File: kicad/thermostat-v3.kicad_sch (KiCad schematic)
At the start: 91 parts, among them J1 HVAC R C W Y G, J2 USB-C, J3 Stemma QT, J4 2.9in EPD FPC, Q1 SI1308EDL, Q2 BT136S-600D, Q3 BT136S-600D, Q4 BT136S-600D, SW1 RESET, SW2 BOOT, SW3 UP, SW4 DOWN, SW5 MODE, U1 LMR16006XDDCR, U2 USBLC6-2SC6, U3 ESP32-C6-WROOM-1-N8, U4 STWD100NYWY3F, U5 SHT40-AD1B, U6 MOC3063S, U7 MOC3063S, U8 MOC3063S

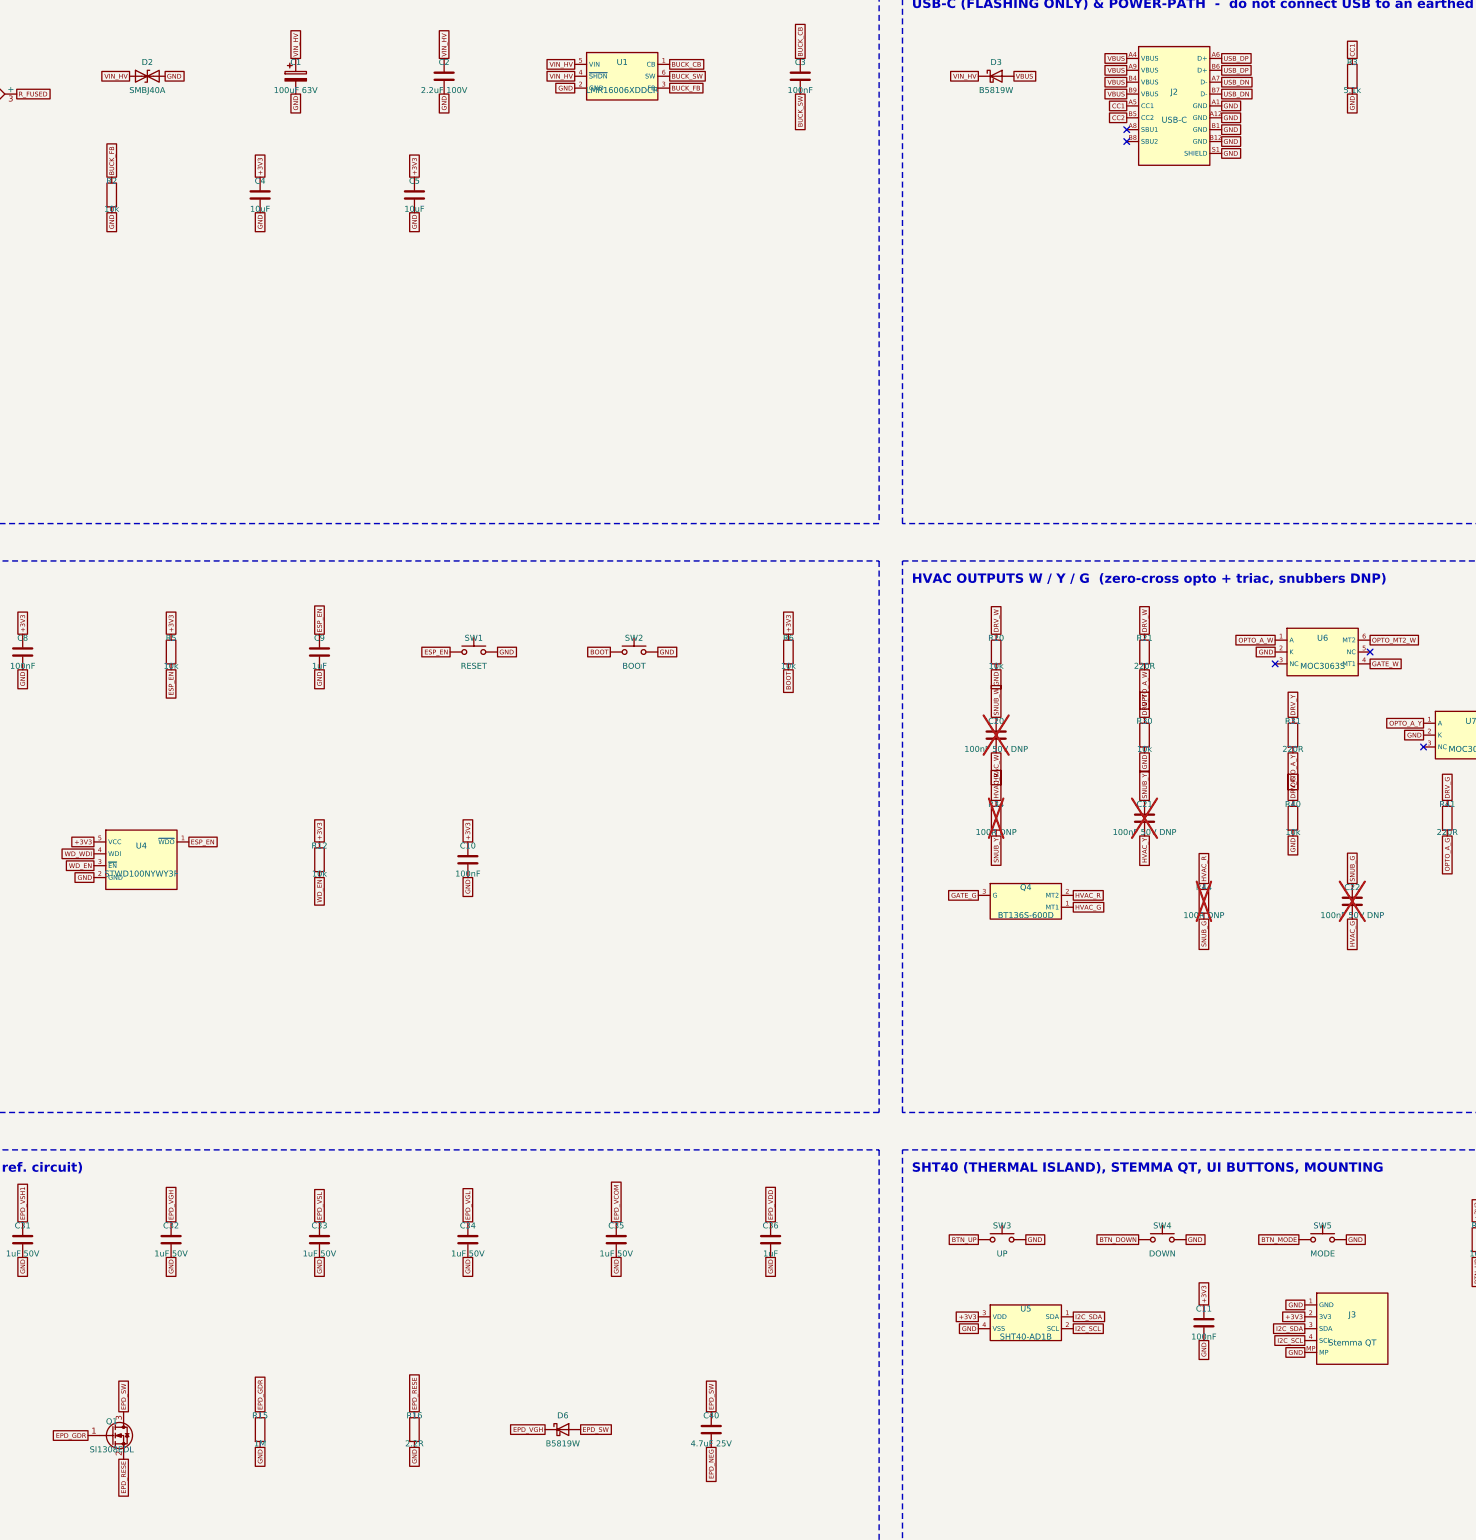
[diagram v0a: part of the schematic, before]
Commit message: V3 rev4: fix CPL/gerber origin, switch BOM grouping, basic-part swaps, silkscreen cleanup, cat logo
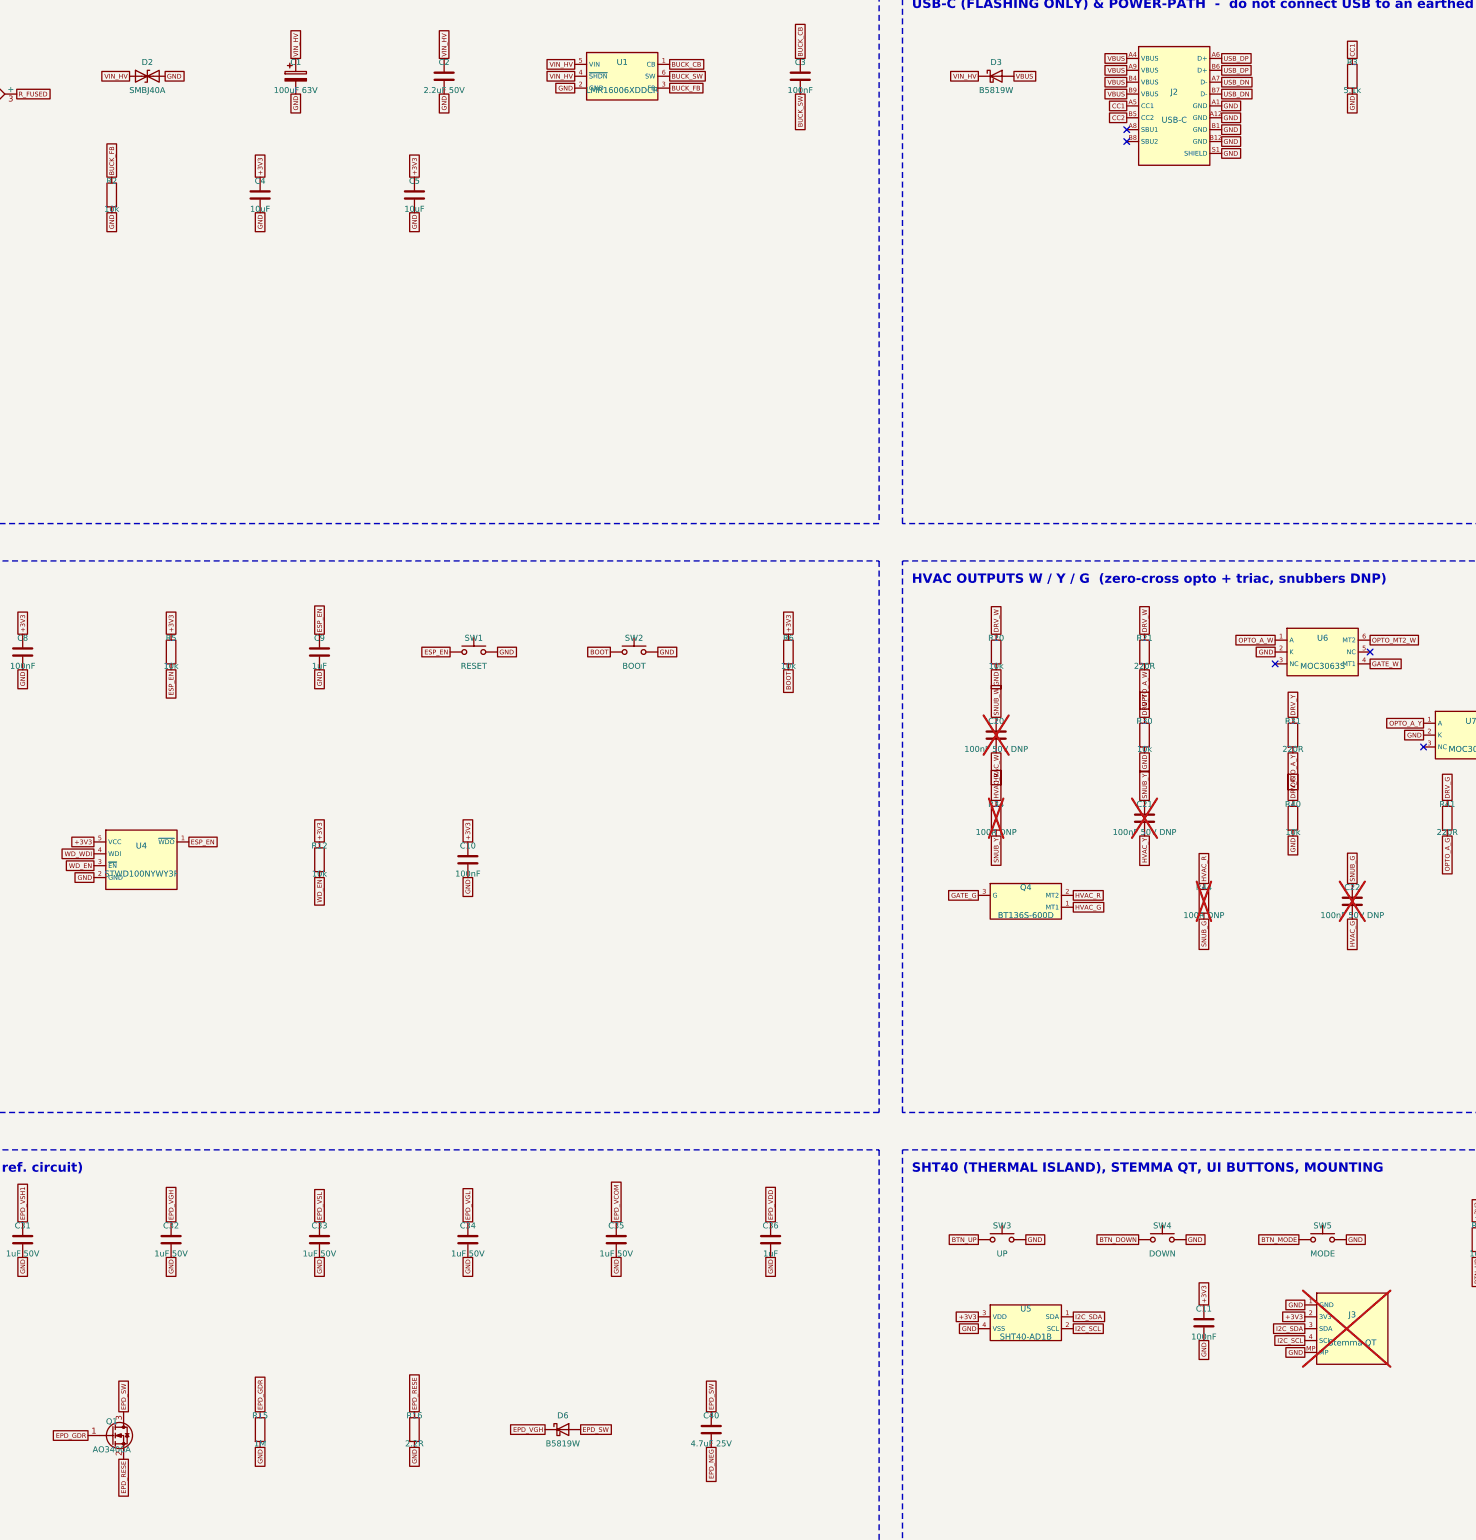
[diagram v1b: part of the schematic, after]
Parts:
- C2: value 2.2uF 100V -> 2.2uF 50V; LCSC C170101 -> C50254
- J3: now not fitted
- Q1: value SI1308EDL -> AO3400A; footprint tstat:SOT-323_SI1308 -> tstat:SOT-23_AO3400A; LCSC C469327 -> C20917
- R16: footprint Resistor_SMD:R_0402_1005Metric -> Resistor_SMD:R_0603_1608Metric; LCSC C25101 -> C22939
- SW1, SW2, SW3, SW4, SW5: footprint Button_Switch_SMD:SW_Push_1P1T_XKB_TS-1187A -> tstat:SW_TS1187A

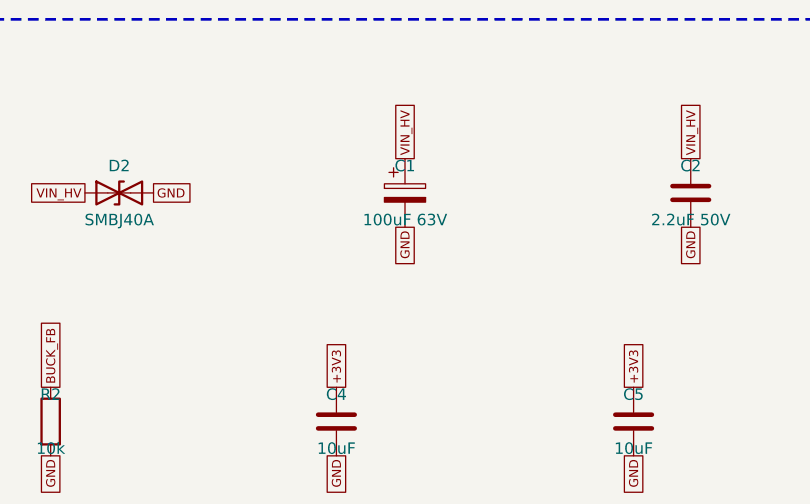
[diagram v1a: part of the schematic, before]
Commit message: V3 rev5: rear vertical HVAC terminal, low-profile C1, SHT40 island net rule, 3D-printable case (OpenSCAD/STL/3MF)
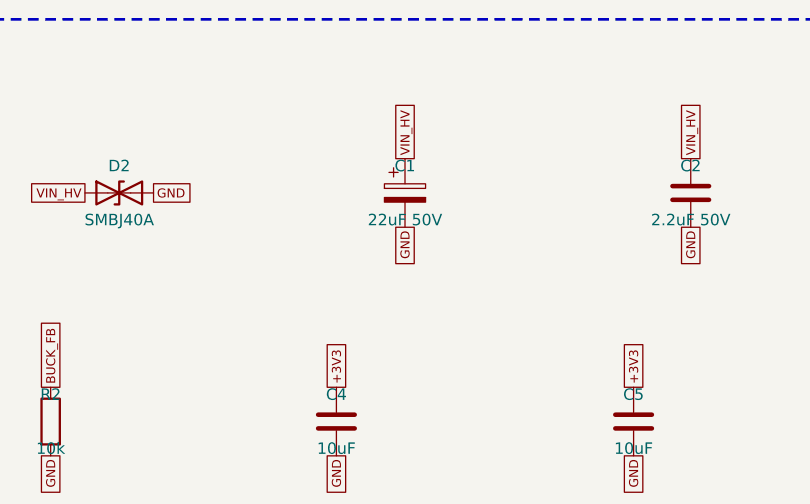
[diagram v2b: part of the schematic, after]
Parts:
- C1: value 100uF 63V -> 22uF 50V; footprint tstat:CP_10x10_RVT -> tstat:CP_6.3x5.4_RVT; LCSC C51953411 -> C72505
- J1: footprint tstat:HVAC_TERM_15EDGRC -> tstat:HVAC_TERM_15EDGVC; LCSC C7603439 -> C5188321; MPN 15EDGRC-3.5-05P (hand-solder) -> MX15EDGVC-3.5-05P + 15EDGK plug (hand-solder, back side)

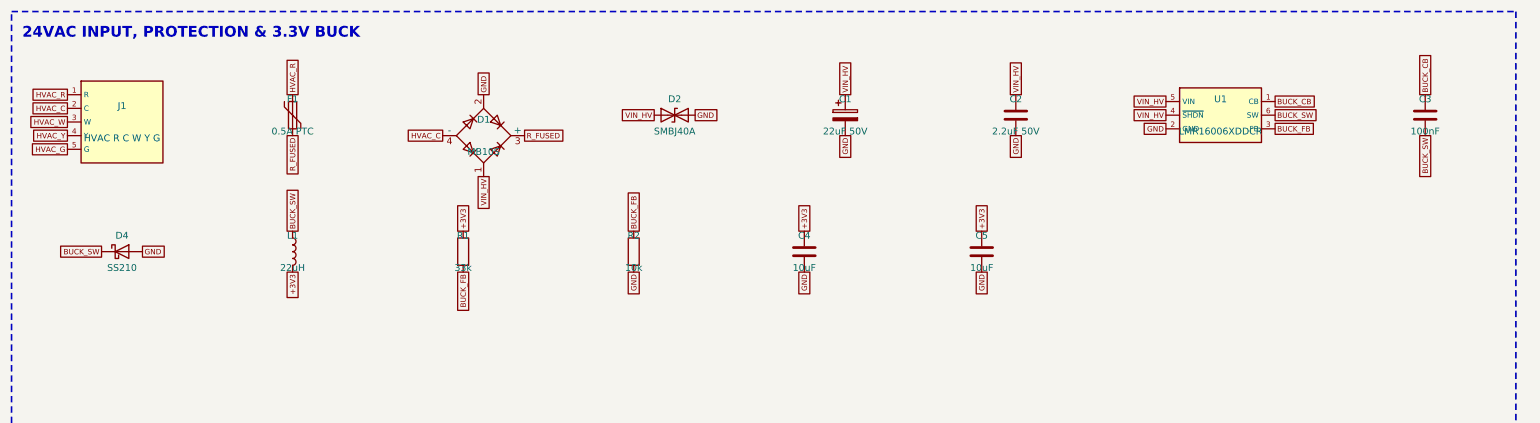
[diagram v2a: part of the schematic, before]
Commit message: V3 rev6: drywall-anchor case (146x70), multi-colour AMS parts + 3MF, no USB opening, 100V X7R bulk caps
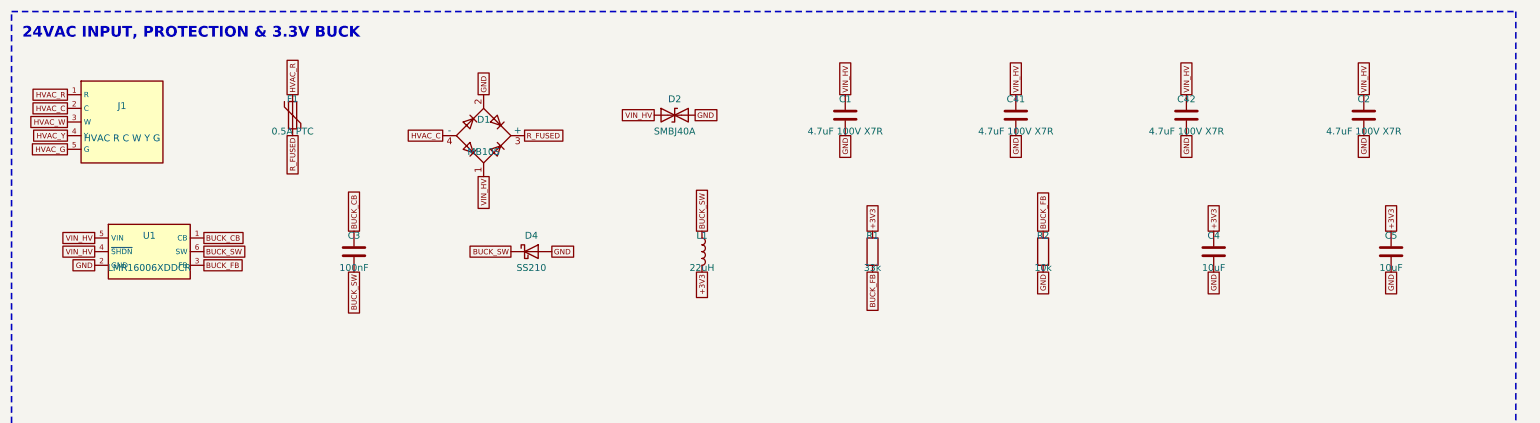
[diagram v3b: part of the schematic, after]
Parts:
- added C41, C42: 4.7uF 100V X7R, Capacitor_SMD:C_1210_3225Metric, symbol Device:C
- C1: value 22uF 50V -> 4.7uF 100V X7R; footprint tstat:CP_6.3x5.4_RVT -> Capacitor_SMD:C_1210_3225Metric; symbol Device:C_Polarized -> Device:C; LCSC C72505 -> C381466; MPN (none) -> FS32X475K101EGG
- C2: value 2.2uF 50V -> 4.7uF 100V X7R; footprint Capacitor_SMD:C_1206_3216Metric -> Capacitor_SMD:C_1210_3225Metric; LCSC C50254 -> C381466; MPN (none) -> FS32X475K101EGG
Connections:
- net GND: now also C41.2, C42.2
- net VIN_HV: now also C41.1, C42.1
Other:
- moved on the sheet: C2, C3, C4, C5, D4, L1, R1, R2, U1

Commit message: V3 rev7: rear right-angle HVAC terminal beside centred wire hole, deeper case standoffs
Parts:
- J1: footprint tstat:HVAC_TERM_15EDGVC -> tstat:HVAC_TERM_15EDGRC; LCSC C5188321 -> C7603439; MPN MX15EDGVC-3.5-05P + 15EDGK plug (hand-solder, back side) -> 15EDGRC-3.5-05P-14-00A(H) right-angle, BACK side, + plug 15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

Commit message: Rev 8: review fixes - J1 really at (70,58) rear, D3 SS210 100V, F1 60V PTC, SHDN 100k, C43 47uF/63V rear THT, T435-600B standard-gate triacs, antenna keepout, USB-C flush, 1mm HV pour clearance, test pads; case RESET pinhole; generator scripts + review response
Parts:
- added C43: 47uF 63V, Capacitor_THT:CP_Radial_D8.0mm_P3.50mm, symbol Device:C_Polarized
- added R50: 100k, Resistor_SMD:R_0402_1005Metric, symbol Device:R
- added TP1: VIN_HV, TestPoint:TestPoint_Pad_D1.5mm, symbol Connector:TestPoint
- added TP2: GND, TestPoint:TestPoint_Pad_D1.5mm, symbol Connector:TestPoint
- added TP3: +3V3, TestPoint:TestPoint_Pad_D1.5mm, symbol Connector:TestPoint
- added TP4: VBUS, TestPoint:TestPoint_Pad_D1.5mm, symbol Connector:TestPoint
- D3: value B5819W -> SS210; footprint tstat:SOD-123_B5819W -> tstat:SMA_SS210; LCSC C8598 -> C14996; MPN (none) -> SS210 100V 2A Schottky (was B5819W 40V)
- F1: value 0.5A PTC -> 0.5A 60V PTC; LCSC C12559 -> C70113; MPN (none) -> mSMD050-60V
- Q2, Q3, Q4: value BT136S-600D -> T435-600B; LCSC C18186224 -> C145128; MPN (none) -> T435-600B-TR (ST, standard-gate snubberless, was BT136S-600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
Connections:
- net +3V3: now also TP3.1
- net GND: now also C43.2, TP2.1
- net VBUS: now also TP4.1
- net VIN_HV: now also C43.1, R50.1, TP1.1; no longer U1.4 (~{SHDN})
- new net BUCK_EN: R50.2, U1.4 (~{SHDN})
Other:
- moved on the sheet: C2, C3, C4, C41, C42, C5, D4, L1, R1, R2, U1

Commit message: Rev 9: R51 3.3R pulse-proof series resistor (bridge->bulk, TVS clamp ~58V at U1), L1 SWPA6045S220MT 22uH Isat 2.2A; regenerated fab (DRC/ERC 0); final review notes; exploded case+PCB renders
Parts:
- added R51: 3.3R 0.75W pulse, Resistor_SMD:R_1206_3216Metric, symbol Device:R
- L1: footprint tstat:L_4030_SWPA -> Inductor_SMD:L_Sunlord_SWPA6045S; LCSC C83472 -> C83454; MPN (none) -> SWPA6045S220MT 22uH Isat 2.2A 89mOhm (was SWPA4030 1.0A)
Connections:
- net VIN_HV: now also R51.2; no longer D1.1
- new net VIN_RECT: D1.1, R51.1
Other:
- moved on the sheet: C1, C2, C3, C4, C41, C42, C43, C5, D2, D4, L1, R1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

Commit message: Rev 11: Q2-Q4 T435-600B -> T405-600B-TR (C283473, IH 10 mA); refresh bom_prices; regen fab
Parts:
- Q2, Q3, Q4: value T435-600B -> T405-600B; LCSC C145128 -> C283473; MPN T435-600B-TR (ST, standard-gate snubberless, was BT136S-600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 -> T405-600B-TR (ST T4 logic-level, IGT 5mA IH 10mA; was T435-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

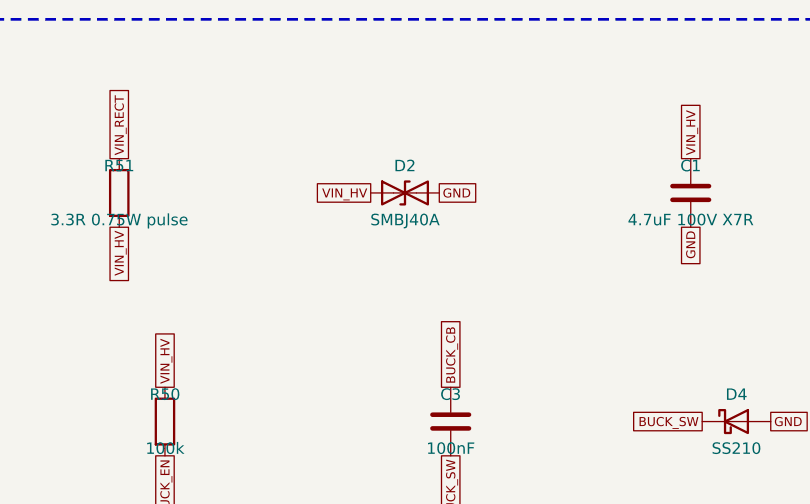
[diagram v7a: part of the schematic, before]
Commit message: Rev 12: D2 SMBJ40A -> SMBJ40CA (JLC preferred-extended, no loading fee); refresh prices
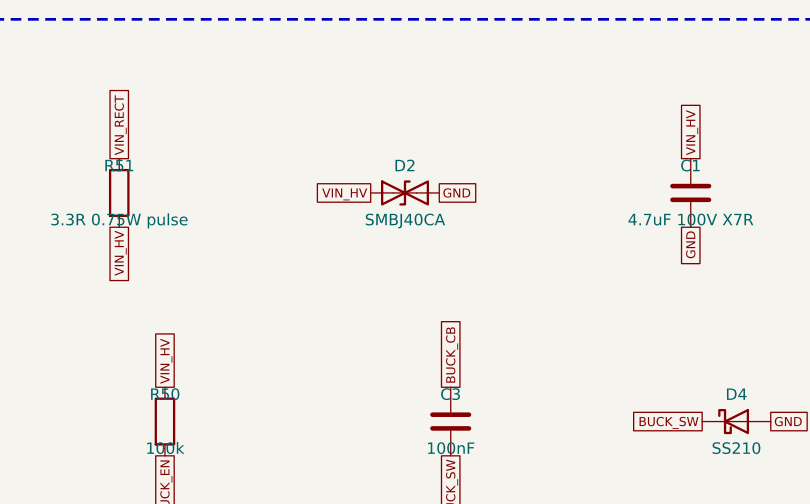
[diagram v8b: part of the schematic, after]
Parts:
- D2: value SMBJ40A -> SMBJ40CA; LCSC C114003 -> C19077590; MPN (none) -> SMBJ40CA (bidirectional, JLC preferred-extended; was SMBJ40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
